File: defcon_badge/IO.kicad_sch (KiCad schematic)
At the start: 9 parts, among them J30 SAO 2x3, J31 microSD, SW20 TS-1187A, SW21 TS-1187A, SW22 TS-1187A, SW23 TS-1187A

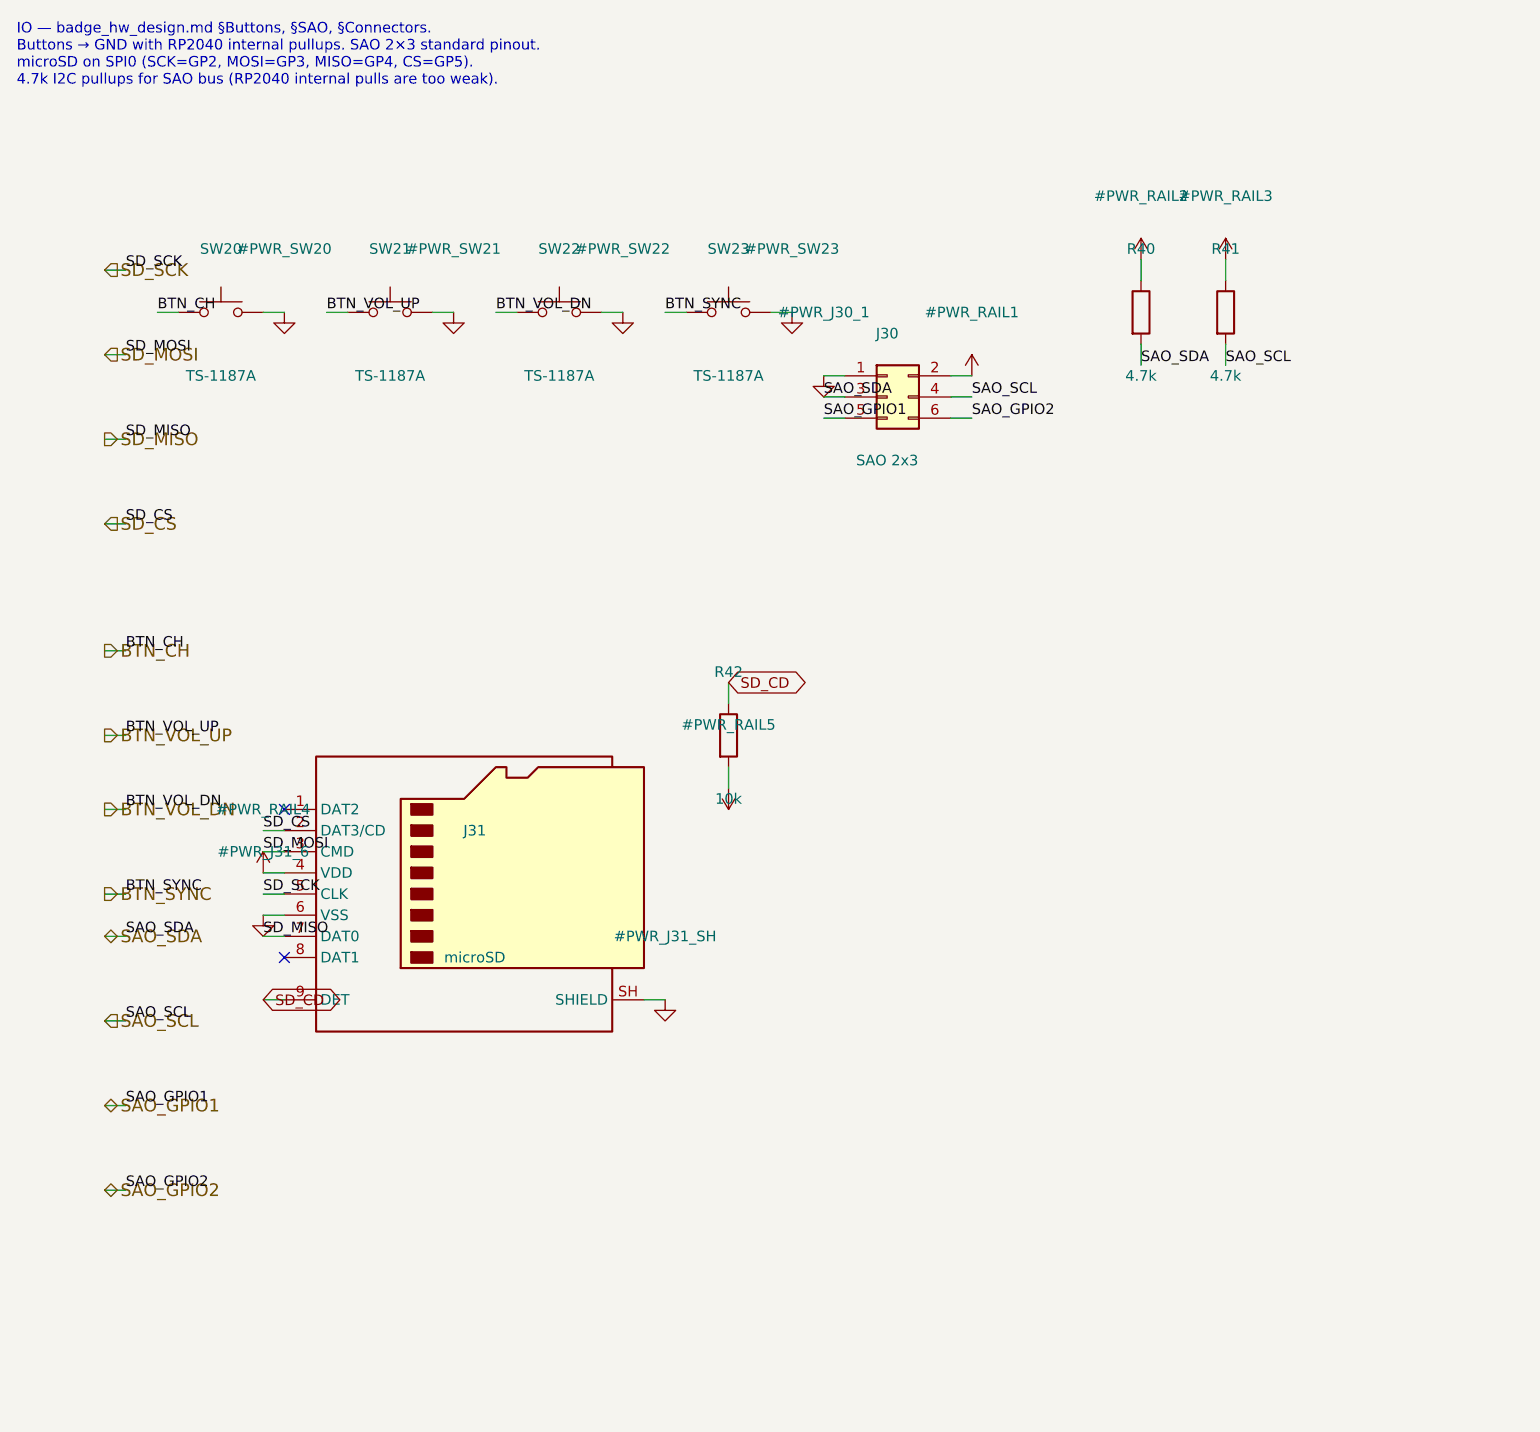
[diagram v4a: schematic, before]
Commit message: Fix 3 pin-out bugs found by the datasheet audit (D20, J30, J31)
Ran a datasheet pin-out audit (verify + adversarial cross-check) over all 18
parts with datasheet-defined pinouts. 14 verified clean. Four flagged; after
independent adjudication, three were real bugs and one a false positive:

D20 IR LED (FATAL, reverse-biased): the Everlight IR15-21C/TR8 datasheet
numbers pad 1 = ANODE, pad 2 = CATHODE — the OPPOSITE of KiCad's stock LED
convention (pad1=cathode). Under standard part-pin1 -> footprint-pad1
placement, the old wiring put the real anode on IR_DRIVE and the cathode on
+3V3, so the emitter could never forward-bias and the IR-sync TX was dead.
ERC-invisible (both pins passive). Also the footprint was 0805 for a 1206
part. Fixed: new badge:LED_IR_1206_3216Metric (pad1=anode, pad2=cathode,
cathode silk on pad 2) + swapped nets (pad1->+3V3, pad2->IR_DRIVE) + correct
1206 land + LCSC C72037->C409499. Nudged inboard for edge clearance.

J30 SAO header (FATAL for add-ons): VCC/GND were swapped vs the SAO 1.69bis
standard (badge.team: pin1=3V3, pin2=GND). A compliant SAO add-on would have
been reverse-powered. Fixed: pin1->+3V3, pin2->GND.

J31 microSD card-detect (broken feature): the Hirose DM3D-SF detect switch is
between pads 9 and 10, but the Det1 symbol exposes only pin 9 -> pad 10 floated,
so inserting a card never pulled SD_CD low. Fixed: Det2 symbol + pin 10 -> GND.

LED22 / SK9822 (FALSE POSITIVE): the audit compared against the SK9822-EC20
(a 2020 part) from a dated note in badge_hw_design.md. The board uses the 5050
SK9822 (chosen for brightness); its footprint pinout (1=DIN 2=CIN 3=GND 4=VDD
5=COUT 6=DOUT) was independently re-verified clean against the Normand Rev.07
and OPSCO 5050 datasheets. Updated the doc + generator (EC20 2020 -> 5050).

Verified: ERC 0 errors, schematic parity 0, overlaps/courtyard/offboard 0,
DRC 0 except the 28 inherent USB-C (J10) mask bridges. Top render confirms.

Co-Authored-By: Claude Opus 4.8 (1M context) <noreply@anthr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
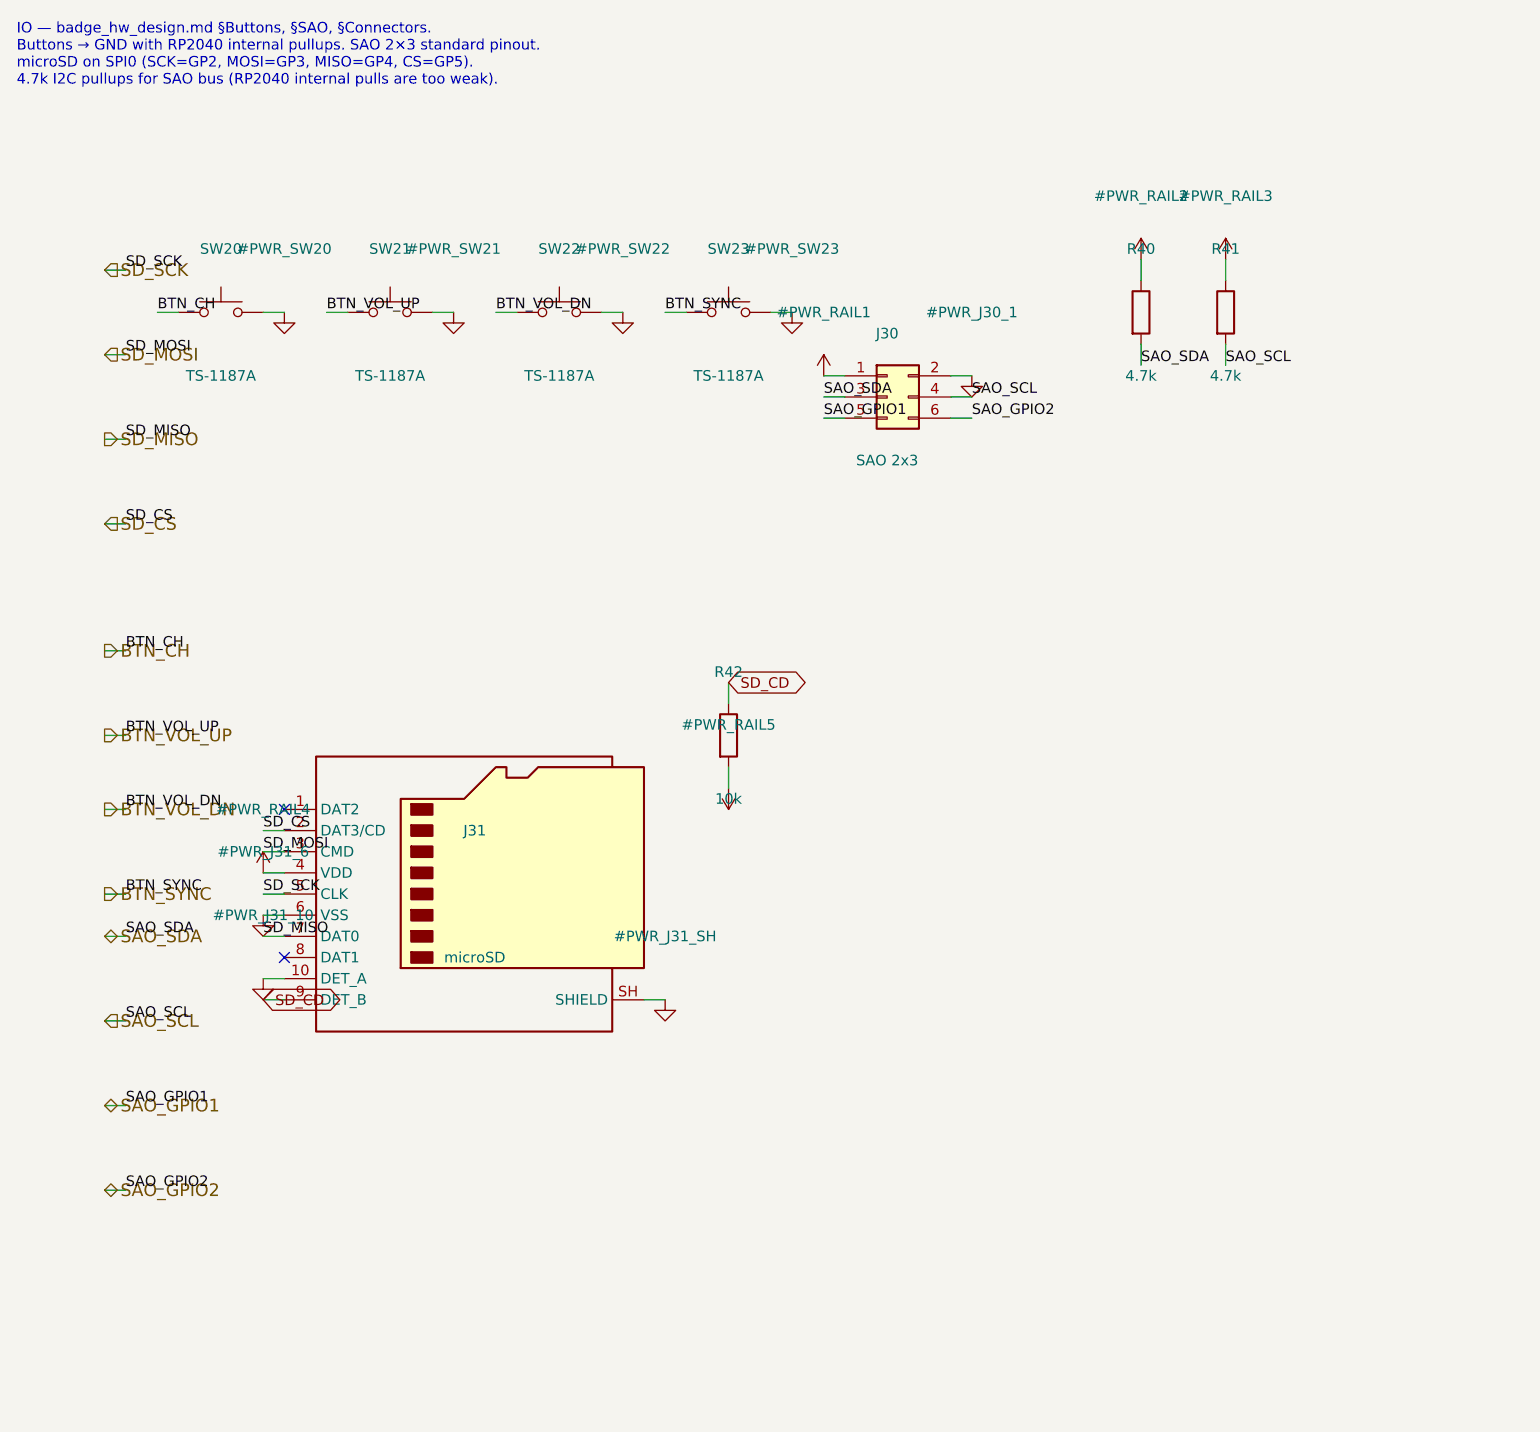
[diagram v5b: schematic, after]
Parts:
- removed J31: microSD, Connector_Card:microSD_HC_Hirose_DM3D-SF, symbol Connector:Micro_SD_Card_Det1
- added J31: microSD, Connector_Card:microSD_HC_Hirose_DM3D-SF, symbol Connector:Micro_SD_Card_Det2
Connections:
- net +3V3: now also J30.1 (Pin_1), J31.4 (VDD); no longer J30.2 (Pin_2)
- net GND: now also J30.2 (Pin_2), J31.10 (DET_A), J31.6 (VSS), J31.SH (SHIELD); no longer J30.1 (Pin_1)
- net SD_CD: now also J31.9 (DET_B)
- net SD_CS: now also J31.2 (DAT3/CD)
- net SD_MISO: now also J31.7 (DAT0)
- net SD_MOSI: now also J31.3 (CMD)
- net SD_SCK: now also J31.5 (CLK)
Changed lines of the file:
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@@
 	)
 	(symbol
-		(lib_id "power:GND")
+		(lib_id "power:+3V3")
 		(at 121.92 67.31 0)
 		(unit 1)
@@
 		(dnp no)
 		(fields_autoplaced yes)
-		(property "Reference" "#PWR_J30_1" (at 121.92 59.69 0) (effects (font (size 1.27 1.27))))
-		(property "Value" "GND" (at 121.92 74.93 0) (effects (font (size 1.27 1.27)) (hide yes)))
+		(property "Reference" "#PWR_RAIL1" (at 121.92 59.69 0) (effects (font (size 1.27 1.27))))
+		(property "Value" "+3V3" (at 121.92 74.93 0) (effects (font (size 1.27 1.27)) (hide yes)))
 		(property "Footprint" "" (at 121.92 67.31 0) (show_name no) (hide yes) (effects (font (size 1.27 1.27))))
 		(property "Datasheet" "" (at 121.92 67.31 0) (show_name no) (hide yes) (effects (font (size 1.27 1.27))))
@@
 			(project "defcon_badge"
 				(path "/8c0b3d8b-46d3-4173-ab1e-a61765f77d61/608539de-722a-4bca-b1da-2c313b60cd6f"
-					(reference "#PWR_J30_1")
-					(unit 1)
-				)
-			)
-		)
-	)
-	(symbol
-		(lib_id "power:+3V3")
+					(reference "#PWR_RAIL1")
+					(unit 1)
+				)
+			)
+		)
+	)
+	(symbol
+		(lib_id "power:GND")
 		(at 139.70 67.31 0)
 		(unit 1)
@@
 		(dnp no)
 		(fields_autoplaced yes)
-		(property "Reference" "#PWR_RAIL1" (at 139.70 59.69 0) (effects (font (size 1.27 1.27))))
-		(property "Value" "+3V3" (at 139.70 74.93 0) (effects (font (size 1.27 1.27)) (hide yes)))
+		(property "Reference" "#PWR_J30_1" (at 139.70 59.69 0) (effects (font (size 1.27 1.27))))
+		(property "Value" "GND" (at 139.70 74.93 0) (effects (font (size 1.27 1.27)) (hide yes)))
 		(property "Footprint" "" (at 139.70 67.31 0) (show_name no) (hide yes) (effects (font (size 1.27 1.27))))
 		(property "Datasheet" "" (at 139.70 67.31 0) (show_name no) (hide yes) (effects (font (size 1.27 1.27))))
@@
 			(project "defcon_badge"
 				(path "/8c0b3d8b-46d3-4173-ab1e-a61765f77d61/608539de-722a-4bca-b1da-2c313b60cd6f"
-					(reference "#PWR_RAIL1")
+					(reference "#PWR_J30_1")
 					(unit 1)
 				)
@@
 	)
 	(symbol
-		(lib_id "Connector:Micro_SD_Card_Det1")
+		(lib_id "Connector:Micro_SD_Card_Det2")
 		(at 80.01 129.54 0)
 		(unit 1)
@@
 		(pin "8")
 		(pin "9")
+		(pin "10")
 		(pin "SH")
 		(instances
@@
 				(path "/8c0b3d8b-46d3-4173-ab1e-a61765f77d61/608539de-722a-4bca-b1da-2c313b60cd6f"
 					(reference "#PWR_J31_6")
+					(unit 1)
+				)
+			)
+		)
+	)
+	(symbol
+		(lib_id "power:GND")
+		(at 54.61 139.70 0)
+		(unit 1)
+		(body_style 1)
+		(exclude_from_sim no)
+		(in_bom yes)
+		(on_board yes)
+		(in_pos_files yes)
+		(dnp no)
+		(fields_autoplaced yes)
+		(property "Reference" "#PWR_J31_10" (at 54.61 132.08 0) (effects (font (size 1.27 1.27))))
+		(property "Value" "GND" (at 54.61 147.32 0) (effects (font (size 1.27 1.27)) (hide yes)))
+		(property "Footprint" "" (at 54.61 139.70 0) (show_name no) (hide yes) (effects (font (size 1.27 1.27))))
+		(property "Datasheet" "" (at 54.61 139.70 0) (show_name no) (hide yes) (effects (font (size 1.27 1.27))))
+		(property "Description" "" (at 54.61 139.70 0) (show_name no) (hide yes) (effects (font (size 1.27 1.27))))
+		(pin "1")
+		(instances
+			(project "defcon_badge"
+				(path "/8c0b3d8b-46d3-4173-ab1e-a61765f77d61/608539de-722a-4bca-b1da-2c313b60cd6f"
+					(reference "#PWR_J31_10")
 					(unit 1)
 				)
@@
 	(wire (pts (xy 57.15 134.62) (xy 54.61 134.62)) (stroke (width 0) (type default)))
 	(wire (pts (xy 57.15 142.24) (xy 54.61 142.24)) (stroke (width 0) (type default)))
+	(wire (pts (xy 57.15 139.70) (xy 54.61 139.70)) (stroke (width 0) (type default)))
 	(wire (pts (xy 100.33 142.24) (xy 102.87 142.24)) (stroke (width 0) (type default)))
 	(wire (pts (xy 110.49 106.68) (xy 110.49 104.14)) (stroke (width 0) (type default)))
